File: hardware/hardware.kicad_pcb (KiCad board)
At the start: 2 copper layers, 127.6 x 90.2 mm, 52 parts, among them J1 USB_C_Receptacle_USB2.0, J2 AudioPlug4, SW1 SW_Push, SW2 SW_Push, SW3 SW_Push, SW4 SW_Push, SW5 SW_Push, SW6 SW_Push, SW7 SW_Push, U1 ProMicro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

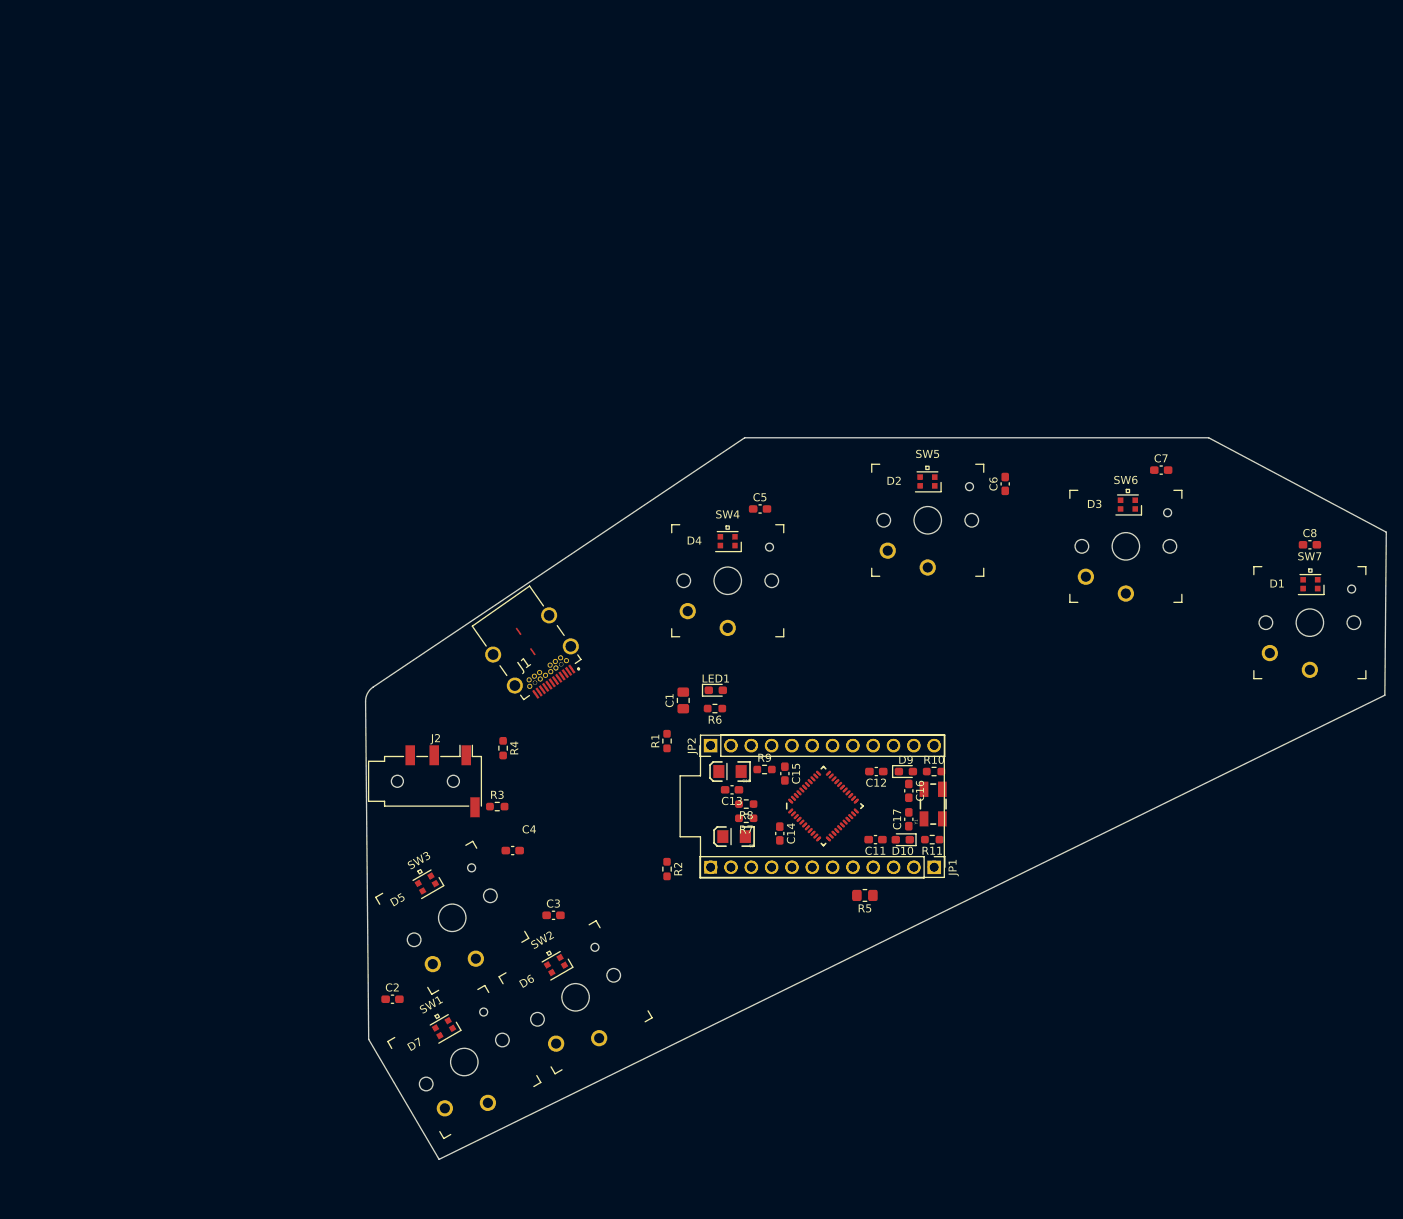
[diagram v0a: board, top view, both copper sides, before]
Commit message: add backside and rounded corners
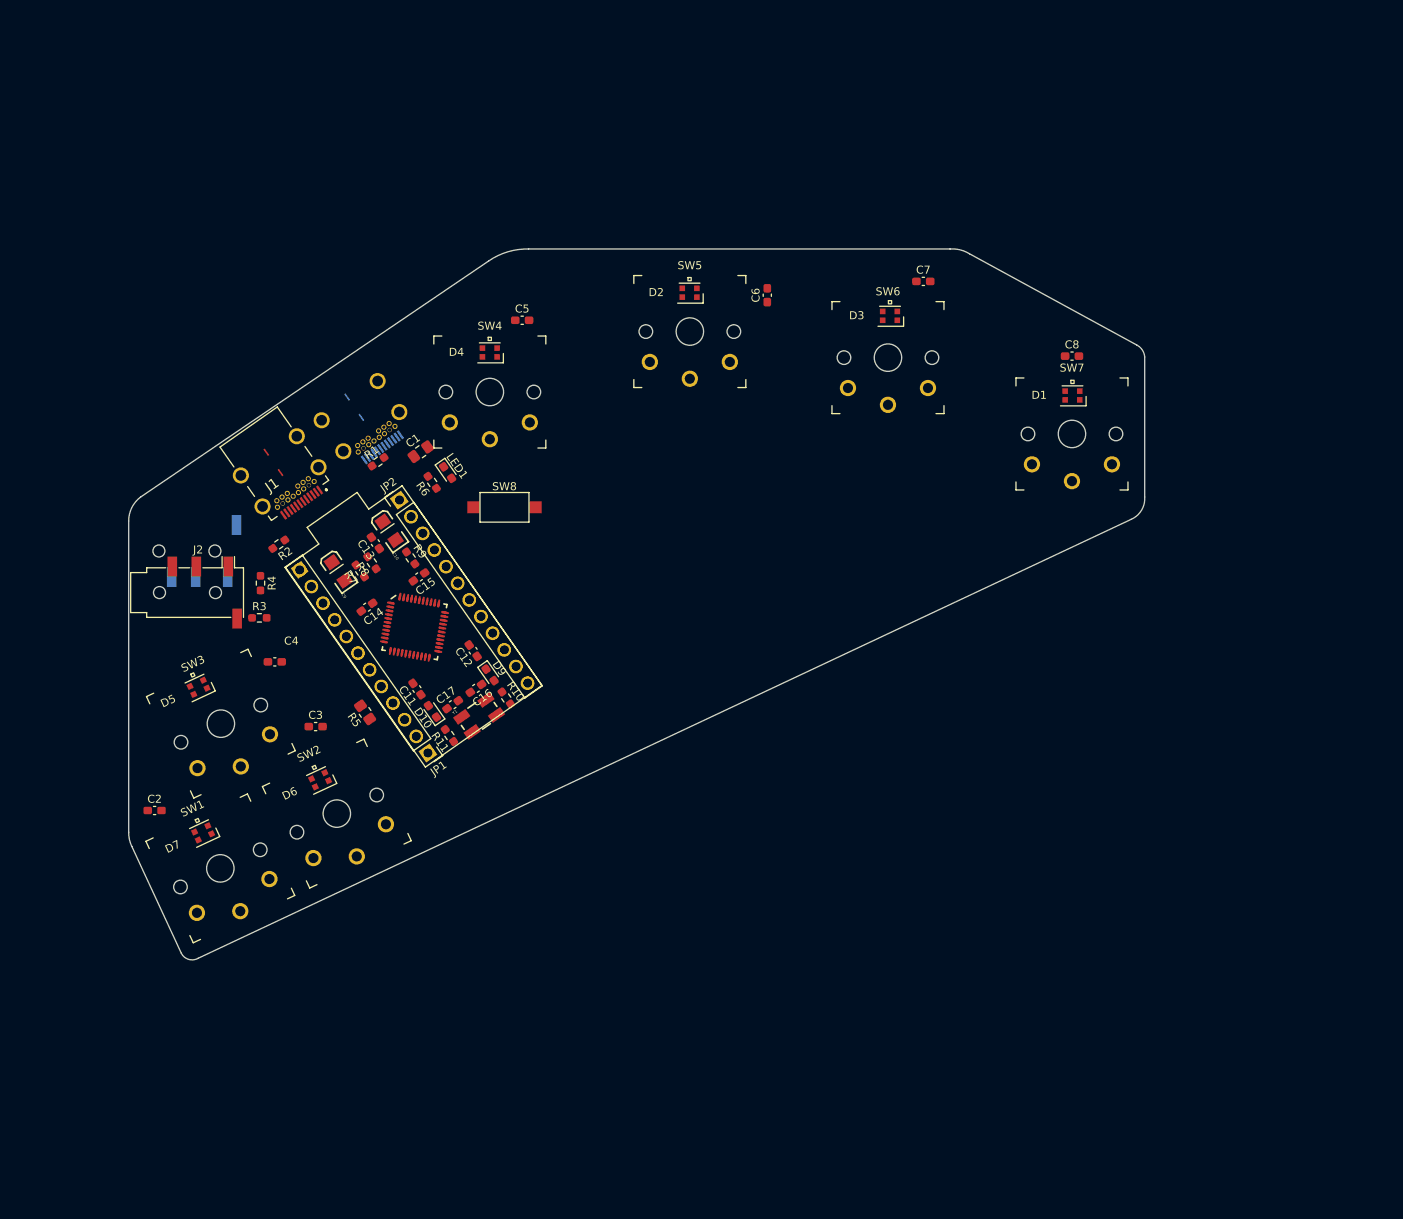
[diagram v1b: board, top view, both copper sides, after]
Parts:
- added J3: USB_C_Receptacle_USB2.0, Library:SS52400002, B.Cu at (28.6, 20.3)
- added J4: AudioPlug4, Connector_Audio:Jack_3.5mm_PJ320D_Horizontal, B.Cu at (8.55, 37.8)
- added SW8: SW_Push, Button_Switch_SMD:SW_SPST_CK_RS282G05A3, F.Cu at (47.0, 32.3)
- moved R5 66.5 mm to (29.5, 57.9), turned to 125 degrees
- moved JP1 64.9 mm to (37.4, 63.0), turned to -145 degrees
- moved R2 63.3 mm to (18.8, 36.9), turned to -145 degrees
- moved R11 61.7 mm to (40.1, 60.8), turned to 125 degrees
- moved D10 60.9 mm to (38.0, 57.8), turned to 125 degrees
- moved C11 60.3 mm to (36.0, 55.0), turned to 125 degrees
- moved C9 59.5 mm to (26.2, 40.3), turned to 125 degrees
- moved C14 58.8 mm to (29.8, 44.8), turned to -145 degrees
- moved C17 58.8 mm to (40.5, 57.0), turned to 35 degrees
- moved Y1 57.8 mm to (43.8, 58.4), turned to 35 degrees
- moved R7 57.3 mm to (28.9, 40.2), turned to 125 degrees
- moved U1 55.8 mm to (35.6, 47.2), turned to -55 degrees
- moved U3 55.8 mm to (35.7, 47.3), turned to -10 degrees
- moved R8 55.7 mm to (30.4, 39.2), turned to 125 degrees
- moved C16 55.6 mm to (43.4, 54.9), turned to -145 degrees
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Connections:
- U1 pad 22: unconnected-(U1-Pad22) -> Net-(U1-Pad22)
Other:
- board size 127.6 x 90.2 mm -> 127 x 88.9 mm

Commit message: start routing
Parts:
- removed U1: ProMicro, Library:ProMicro
- moved C2 40.1 mm to (-0.07, 30.3), turned to -35 degrees
- moved SW1 37.6 mm to (2.51, 40.9), turned to -10 degrees
- moved D7 37.4 mm to (3.29, 36.0), turned to -10 degrees
- moved C8 37.1 mm to (126.4, 49.5), turned to -35 degrees
- moved D1 35.7 mm to (123.7, 53.6), turned to -35 degrees
- moved SW7 34.5 mm to (120.9, 57.5), turned to -35 degrees
- moved D5 34.3 mm to (13.5, 20.8), turned to -10 degrees
- moved J2 33.9 mm to (20.0, 11.0), turned to -35 degrees
- moved SW3 33.2 mm to (13.2, 26.2), turned to -10 degrees
- moved R2 32.3 mm to (39.9, 12.4), turned to 180 degrees
- moved C7 32.2 mm to (116.6, 31.2), turned to -35 degrees
- moved J1 29.9 mm to (37.1, 3.78), turned to 180 degrees
- moved R4 29.2 mm to (27.1, 14.6), turned to -125 degrees
- moved R3 29.2 mm to (24.6, 18.1), turned to -35 degrees
- moved J4 29.1 mm to (20.0, 11.0), turned to -35 degrees
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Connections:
- J1 pad B5: Net-(J1-PadB5) -> Net-(J3-PadB5)
- J2 pad T: BTN1 -> SCK
- J3 pad A5: GND -> Net-(J1-PadA5)
- J3 pad B5: GND -> Net-(J3-PadB5)
- J4 pad T: BTN1 -> SCK
- JP1 pad 7: BTN1 -> SCK
- R1 pad 1: Net-(J1-PadA5) -> Net-(J3-PadB5)
- R2 pad 1: Net-(J1-PadB5) -> GND
- R2 pad 2: GND -> Net-(J1-PadA5)
- R4 pad 1: BTN1 -> SCK
- R5 pad 1: Net-(R5-Pad1) -> GND
- R5 pad 2: GND -> /Pro Micro/D8
- SW8 pad 1: Net-(U1-Pad22) -> /Pro Micro/RESET
- U3 pad 18: BTN1 -> SCK
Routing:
- net +5V: track 0.00 -> 144.9 mm, vias 0 -> 12
- net GND: track 0.00 -> 50.6 mm, vias 0 -> 5
- net USB_D+: track 0.00 -> 33.4 mm, vias 0 -> 2
- net /Pro Micro/D8: track 0.00 -> 32.8 mm, vias 0 -> 1
- net USB_D-: track 0.00 -> 32.6 mm, vias 0 -> 1
- net LED_IN: track 0.00 -> 28.6 mm, vias 0 -> 1
- net Net-(J3-PadB5): track 0.00 -> 23.7 mm
- net /Pro Micro/TXO: track 0.00 -> 23.5 mm, vias 0 -> 2
- net BTN4: track 0.00 -> 23.1 mm, vias 0 -> 2
- net /Pro Micro/RESET: track 0.00 -> 22.0 mm, vias 0 -> 2
- net /Pro Micro/RXI: track 0.00 -> 21.6 mm, vias 0 -> 2
- net BTN2: track 0.00 -> 21.3 mm, vias 0 -> 1
- net /Pro Micro/D14: track 0.00 -> 20.8 mm, vias 0 -> 2
- net BTN3: track 0.00 -> 19.8 mm, vias 0 -> 1
- net BTN1: track 0.00 -> 17.3 mm, vias 0 -> 1
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- added copper zone on B.Cu, net GND
- added copper zone on F.Cu, net GND
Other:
- board size 127 x 88.9 mm -> 141.7 x 73.6 mm
- board text added: "Reset"

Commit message: finish routing
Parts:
- removed R7, R8: 22, Resistor_SMD:R_0603_1608Metric_Pad0.98x0.95mm_HandSolder
- added C18: LED, Capacitor_SMD:C_0603_1608Metric_Pad1.08x0.95mm_HandSolder, B.Cu at (116.9, 31.1)
- added C19: LED, Capacitor_SMD:C_0603_1608Metric_Pad1.08x0.95mm_HandSolder, B.Cu at (124.4, 47.3)
- added C20: LED, Capacitor_SMD:C_0603_1608Metric_Pad1.08x0.95mm_HandSolder, B.Cu at (67.4, 1.52)
- added C21: LED, Capacitor_SMD:C_0603_1608Metric_Pad1.08x0.95mm_HandSolder, B.Cu at (82.3, 12.5)
- added C22: LED, Capacitor_SMD:C_0603_1608Metric_Pad1.08x0.95mm_HandSolder, B.Cu at (22.4, 33.2)
- added C23: LED, Capacitor_SMD:C_0603_1608Metric_Pad1.08x0.95mm_HandSolder, B.Cu at (0.92, 30.7)
- added C24: LED, Capacitor_SMD:C_0603_1608Metric_Pad1.08x0.95mm_HandSolder, B.Cu at (11.6, 16.8)
- added D11: WS2812B, Library:LED_WS2812B_PLCC4_2.2x2.2mm, B.Cu at (110.2, 32.6)
- added D12: WS2812B, Library:LED_WS2812B_PLCC4_2.2x2.2mm, B.Cu at (91.9, 15.8)
- added D13: WS2812B, Library:LED_WS2812B_PLCC4_2.2x2.2mm, B.Cu at (66.9, 7.54)
- added D14: WS2812B, Library:LED_WS2812B_PLCC4_2.2x2.2mm, B.Cu at (19.2, 38.9)
- added D15: WS2812B, Library:LED_WS2812B_PLCC4_2.2x2.2mm, B.Cu at (3.36, 36.2)
- added D16: WS2812B, Library:LED_WS2812B_PLCC4_2.2x2.2mm, B.Cu at (14.0, 21.5)
- added D8: WS2812B, Library:LED_WS2812B_PLCC4_2.2x2.2mm, B.Cu at (123.6, 53.6)
- added G***: LOGO, LOGO, F.Cu at (72.7, 57.0)
- added G***: LOGO, LOGO, B.Cu at (72.8, 57.0)
- added R12: 22, Resistor_SMD:R_0603_1608Metric_Pad0.98x0.95mm_HandSolder, F.Cu at (38.0, 20.2)
- added R13: 22, Resistor_SMD:R_0603_1608Metric_Pad0.98x0.95mm_HandSolder, F.Cu at (38.1, 15.5)
- added R14: 22, Resistor_SMD:R_0603_1608Metric_Pad0.98x0.95mm_HandSolder, F.Cu at (40.1, 20.2)
- added R15: 22, Resistor_SMD:R_0603_1608Metric_Pad0.98x0.95mm_HandSolder, F.Cu at (40.1, 15.5)
- added R17: 5.1k, Resistor_SMD:R_0603_1608Metric_Pad0.98x0.95mm_HandSolder, F.Cu at (48.6, 3.97)
- added REF**: MountingHole_3.2mm_M3_ISO7380_Pad, MountingHole:MountingHole_3.2mm_M3_ISO7380_Pad, F.Cu at (122.0, 40.0)
- added REF**: MountingHole_3.2mm_M3_ISO7380_Pad, MountingHole:MountingHole_3.2mm_M3_ISO7380_Pad, F.Cu at (88.0, 60.0)
- added REF**: MountingHole_3.2mm_M3_ISO7380_Pad, MountingHole:MountingHole_3.2mm_M3_ISO7380_Pad, F.Cu at (80.0, 8.00)
- added REF**: MountingHole_3.2mm_M3_ISO7380_Pad, MountingHole:MountingHole_3.2mm_M3_ISO7380_Pad, F.Cu at (25.0, 2.00)
- added SW9: SW_Push, Button_Switch_SMD:SW_SPST_CK_RS282G05A3, B.Cu at (56.7, 23.8)
- moved D3 25.0 mm to (91.9, 15.8)
- moved D2 25.0 mm to (110.2, 32.6)
- moved C6 19.5 mm to (82.3, 12.5), turned to 0 degrees
- moved D5 19.0 mm to (19.2, 38.9)
- moved D7 18.1 mm to (14.0, 21.5)
- moved D6 15.9 mm to (3.36, 36.2)
- moved C4 14.2 mm to (11.6, 16.8), turned to 0 degrees
- moved J3 9.64 mm to (39.6, 3.66)
- moved R2 7.79 mm to (47.5, 10.8)
- moved C5 7.20 mm to (67.4, 1.52), turned to 0 degrees
- moved C8 3.02 mm to (124.4, 47.3), turned to 0 degrees
- moved R1 2.66 mm to (32.5, 5.87)
- moved J1 2.60 mm to (39.6, 3.66)
- moved R3 2.56 mm to (25.0, 20.7), turned to 55 degrees
- moved C2 1.06 mm to (0.91, 30.7), turned to 180 degrees
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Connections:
- J1 pad A6: USB_D+ -> Net-(R15-Pad1)
- J1 pad A7: USB_D- -> Net-(J3-PadA6)
- J1 pad B4: +5V -> unconnected-(J1-PadB4)
- J1 pad B5: Net-(J3-PadB5) -> Net-(J1-PadB5)
- J1 pad B6: USB_D+ -> Net-(R15-Pad1)
- J1 pad B7: USB_D- -> Net-(J3-PadA6)
- J1 pad B8: unconnected-(J1-PadB8) -> Net-(J1-PadB8)
- J1 pad B9: +5V -> unconnected-(J1-PadB9)
- J3 pad A6: USB_D+ -> Net-(J3-PadA6)
- J3 pad A7: USB_D- -> Net-(R15-Pad1)
- J3 pad B4: +5V -> unconnected-(J3-PadB4)
- J3 pad B5: Net-(J3-PadB5) -> Net-(J1-PadB8)
- J3 pad B6: USB_D+ -> Net-(J3-PadA6)
- J3 pad B7: USB_D- -> Net-(R15-Pad1)
- J3 pad B8: unconnected-(J3-PadB8) -> Net-(J1-PadB5)
- J3 pad B9: +5V -> unconnected-(J3-PadB9)
- JP1 pad 3: BTN4 -> /Pro Micro/D7
- JP1 pad 4: BTN5 -> BTN6
- JP1 pad 5: BTN6 -> BTN7
- JP1 pad 6: BTN7 -> BTN5
- JP2 pad 12: /Pro Micro/D10 -> BTN1
- JP2 pad 9: BTN1 -> BTN4
- R1 pad 1: Net-(J3-PadB5) -> Net-(J1-PadB5)
- U3 pad 1: BTN4 -> /Pro Micro/D7
- U3 pad 25: BTN7 -> BTN5
- U3 pad 27: BTN5 -> BTN6
- U3 pad 3: /Pro Micro/D- -> USB_D-
- U3 pad 30: /Pro Micro/D10 -> BTN1
- U3 pad 31: BTN6 -> BTN7
- U3 pad 4: /Pro Micro/D+ -> USB_D+
- U3 pad 9: BTN1 -> BTN4
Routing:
- net +5V: track 144.9 -> 367.5 mm, vias 12 -> 26
- net Net-(D4-Pad4): track 0.00 -> 92.4 mm, vias 0 -> 2
- net BTN1: track 17.3 -> 91.8 mm, vias 1 -> 0
- net BTN2: track 21.3 -> 78.2 mm
- net BTN3: track 19.8 -> 66.4 mm
- net BTN7: track 12.7 -> 55.1 mm, vias 1 -> 2
- net LED_IN: track 28.6 -> 68.8 mm, vias 1 -> 2
- net Net-(D3-Pad4): track 0.00 -> 35.0 mm, vias 0 -> 2
- net Net-(D1-Pad4): track 0.00 -> 32.4 mm, vias 0 -> 2
- net SDA: track 13.9 -> 44.4 mm, vias 1 -> 3
- net Net-(D2-Pad4): track 0.00 -> 30.1 mm, vias 0 -> 3
- net SCK: track 9.78 -> 39.2 mm, vias 1 -> 3
- net Net-(D14-Pad4): track 0.00 -> 27.2 mm, vias 0 -> 3
- net Net-(J3-PadB5): track 23.7 -> 0.00 mm
- net /Pro Micro/D7: track 0.00 -> 23.1 mm, vias 0 -> 2
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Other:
- board text added: ":)"
- board text added: "V3"
- board text added: "github.com/ luksab/keychordz"

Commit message: oder V3
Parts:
- added D+: PinHeader_1x01_P2.54mm_Vertical, Connector_PinHeader_2.54mm:PinHeader_1x01_P2.54mm_Vertical, F.Cu at (30.6, 17.6)
- added D-: PinHeader_1x01_P2.54mm_Vertical, Connector_PinHeader_2.54mm:PinHeader_1x01_P2.54mm_Vertical, F.Cu at (37.7, 16.5)
- moved C2 11.4 mm to (-0.61, 42.0), turned to -170 degrees
- moved C23 11.4 mm to (-0.61, 42.0), turned to -170 degrees
- moved SW1 10.9 mm to (2.74, 51.8), turned to 0 degrees
- moved D15 10.8 mm to (2.77, 47.1), turned to 180 degrees
- moved D6 10.8 mm to (2.77, 47.1), turned to 0 degrees
- moved C24 10.5 mm to (7.51, 26.5), turned to 10 degrees
- moved C4 10.5 mm to (7.51, 26.5), turned to 10 degrees
- moved C19 10.4 mm to (123.9, 37.0), turned to 10 degrees
- moved C8 10.4 mm to (123.9, 37.0), turned to 10 degrees
- moved D1 10.3 mm to (124.2, 43.3), turned to -25 degrees
- moved D8 10.3 mm to (124.2, 43.3), turned to 155 degrees
- moved REF** 10.2 mm to (18.1, 9.59), turned to 10 degrees
- moved SW7 9.98 mm to (122.2, 47.6), turned to -25 degrees
- moved REF** 9.98 mm to (120.3, 30.2), turned to 10 degrees
- moved J2 9.83 mm to (14.8, 19.3), turned to -25 degrees
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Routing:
- net Net-(R15-Pad1): track 14.6 -> 18.6 mm
- net Net-(J3-PadA6): track 14.4 -> 17.8 mm
- net Net-(J1-PadB5): track 7.61 -> 8.38 mm
- net Net-(D4-Pad4): track 92.4 -> 91.8 mm
- net GND: track 66.1 -> 66.2 mm, vias 29 -> 31
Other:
- board size 141.7 x 73.6 mm -> 140.8 x 64.5 mm
- board text added: "Back"
- board text added: "JLCJLCJLCJLC"
- board text added: "Top"
